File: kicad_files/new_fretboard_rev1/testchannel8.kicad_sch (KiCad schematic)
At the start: 22 parts, among them U9 LX3302AQPW-TR-EASY

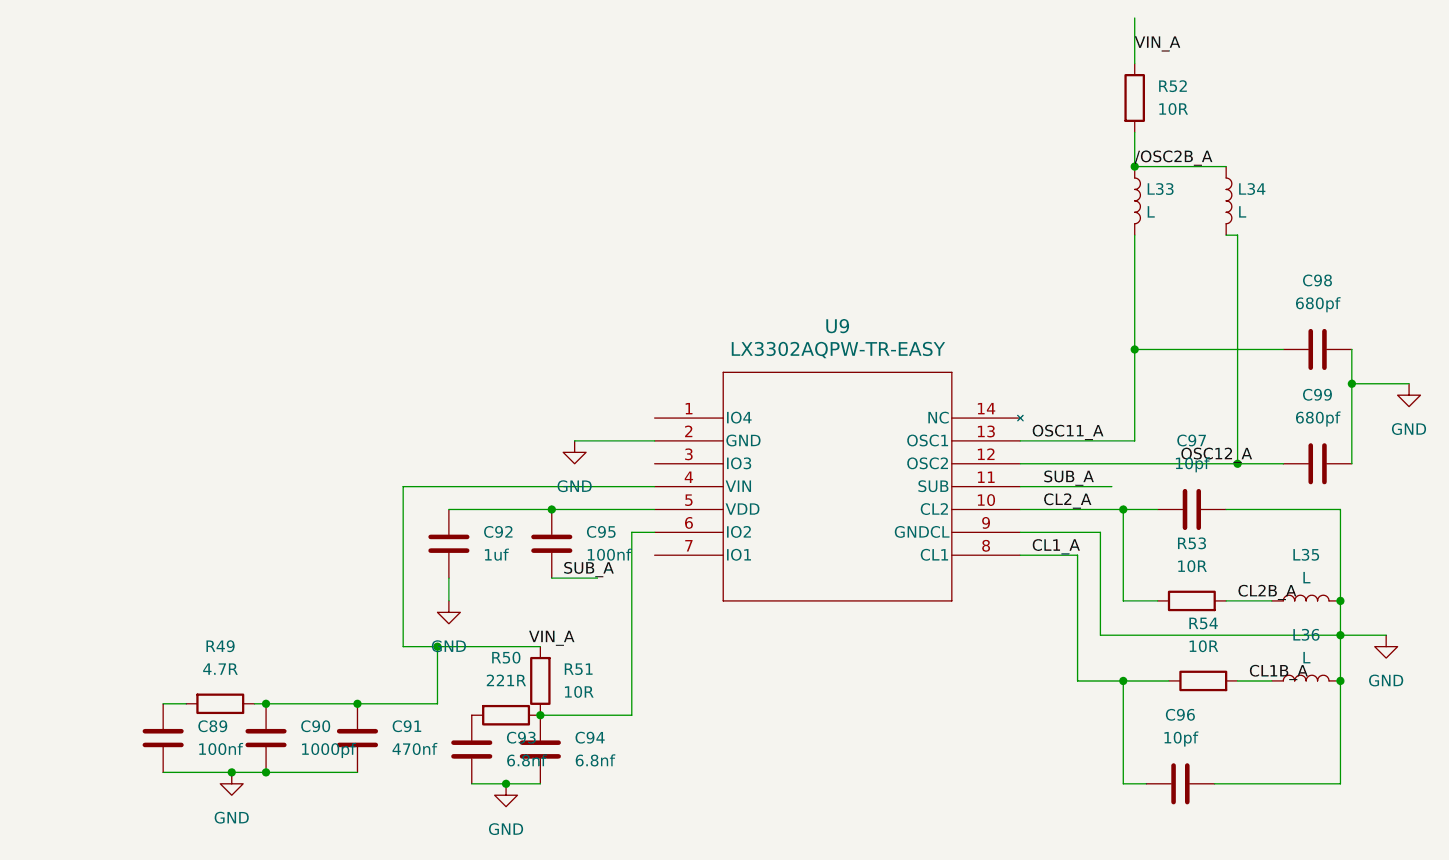
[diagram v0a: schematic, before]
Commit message: stm32 micro added
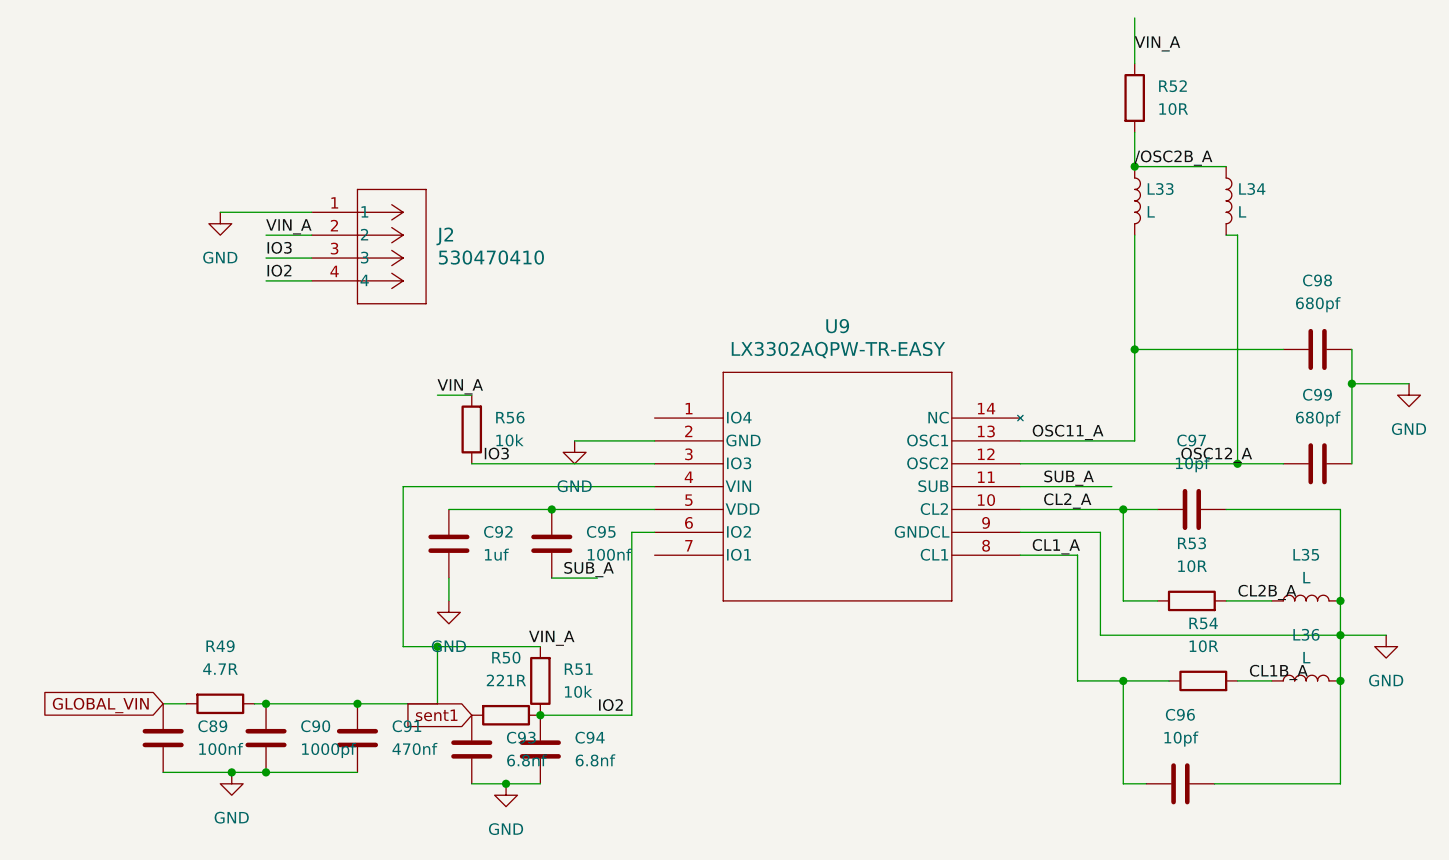
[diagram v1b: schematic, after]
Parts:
- added J2: 530470410, Snapeda:CONN04_530470410_MOL, symbol Snapeda:530470410
- added R56: 10k, Resistor_SMD:R_0402_1005Metric, symbol Device:R
- R51: value 10R -> 10k
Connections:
- net GND: now also J2.1
- net VIN_A: now also J2.2, R56.2
- net IO2: now reaches C94.2, R50.1, R51.1, U9.6 (IO2)
- net IO2: now also J2.4
- net sent1: now reaches C93.2, R50.2
- net GLOBAL_VIN: now reaches C89.2, R49.2
- net IO3: now reaches U9.3 (IO3)
- net IO3: now also J2.3, R56.1

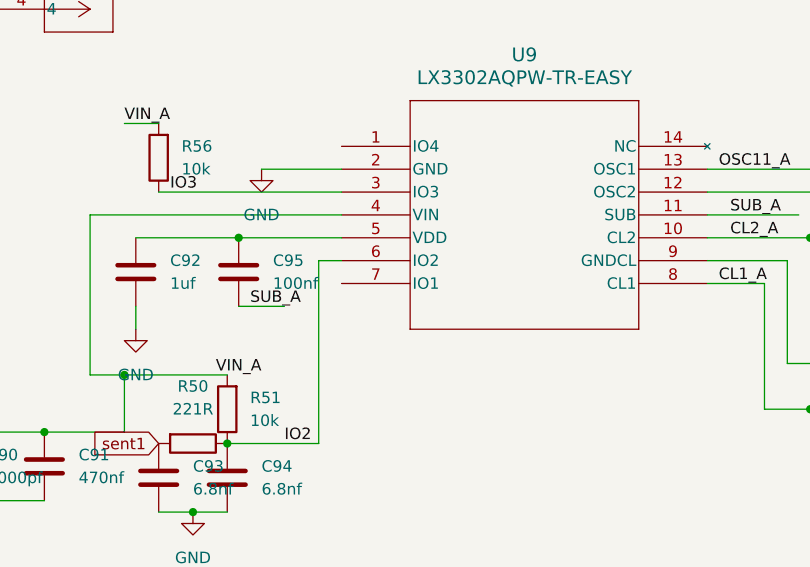
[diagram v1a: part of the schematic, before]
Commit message: mcu configured, still needs power connections and spi i2c connections
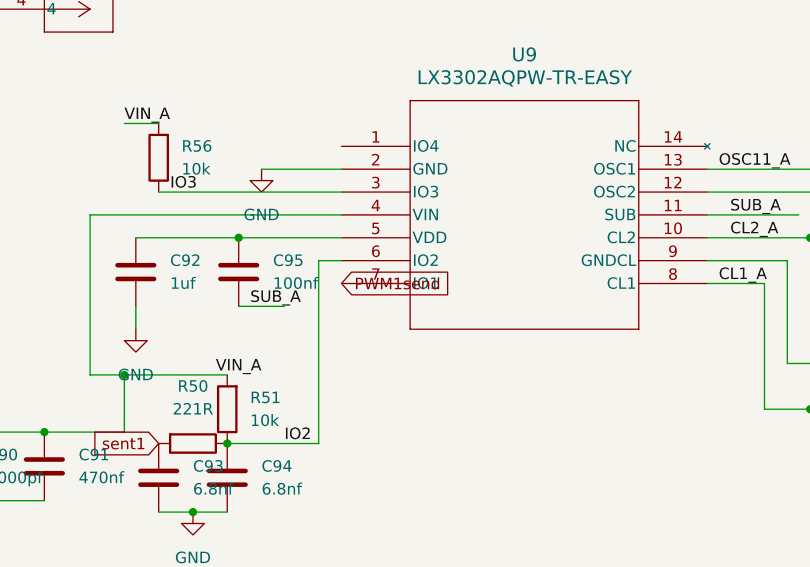
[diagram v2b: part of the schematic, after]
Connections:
- net PWM1send: now reaches U9.7 (IO1)
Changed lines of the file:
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@@
+		)
+	)
+	(global_label "PWM1send"
+		(shape input)
+		(at 105.41 107.95 0)
+		(fields_autoplaced yes)
+		(effects
+			(font
+				(size 1.27 1.27)
+			)
+			(justify left)
+		)
+		(property "Intersheetrefs" "${INTERSHEET_REFS}"
+			(at 118.1922 107.95 0)
+			(effects
+				(font
+					(size 1.27 1.27)
+				)
+				(justify left)
+				(hide yes)
+			)
 		)
 	)

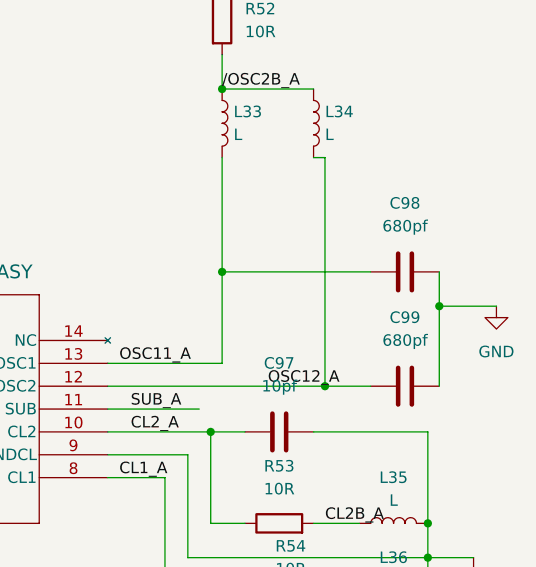
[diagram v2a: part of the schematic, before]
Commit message: mostly done, adjusting silkscreen labels
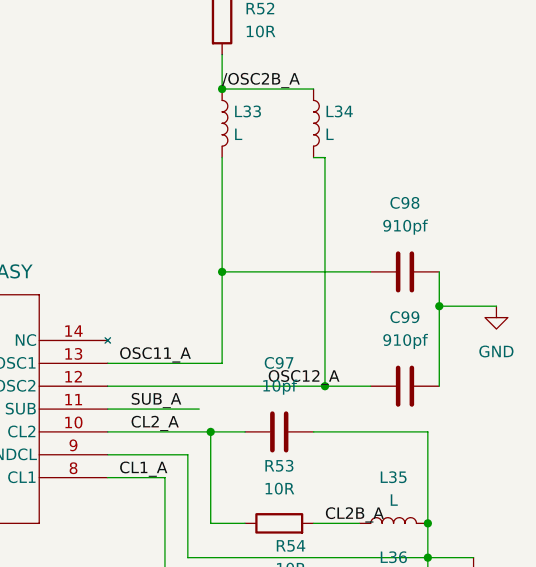
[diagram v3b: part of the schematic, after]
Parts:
- C98, C99: value 680pf -> 910pf
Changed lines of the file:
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@@
 			)
 		)
-		(property "Value" "680pf"
+		(property "Value" "910pf"
 			(at 179.07 80.01 90)
 			(effects
@@
 			)
 		)
-		(property "Value" "680pf"
+		(property "Value" "910pf"
 			(at 179.07 92.71 90)
 			(effects

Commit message: exported gerbers of lefthand
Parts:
- L33, L34, L35, L36: now left out of the parts list
